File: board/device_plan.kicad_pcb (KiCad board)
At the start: 2 copper layers, 29 parts, among them J1 USB, U1 ATTINY2313, x1 12M

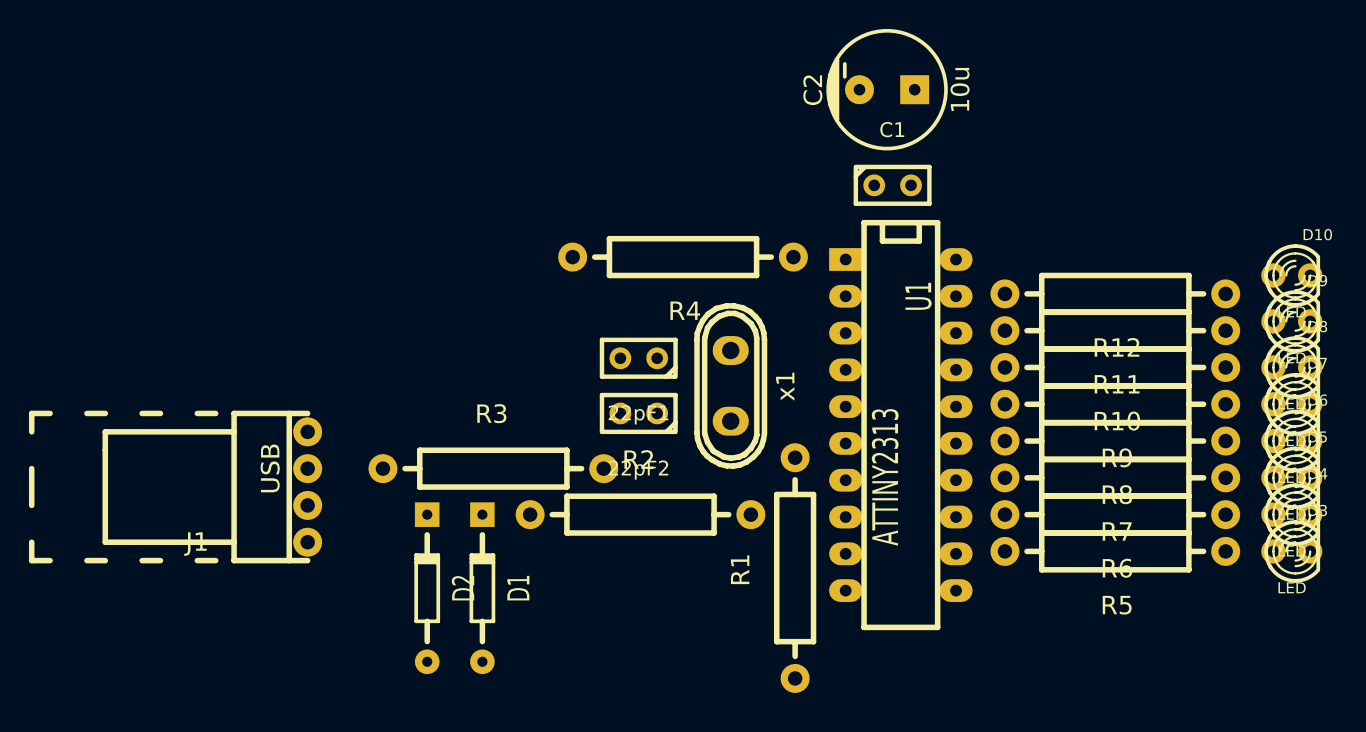
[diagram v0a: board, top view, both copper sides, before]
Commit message: Laid traces on pcb. Added .gitignore.
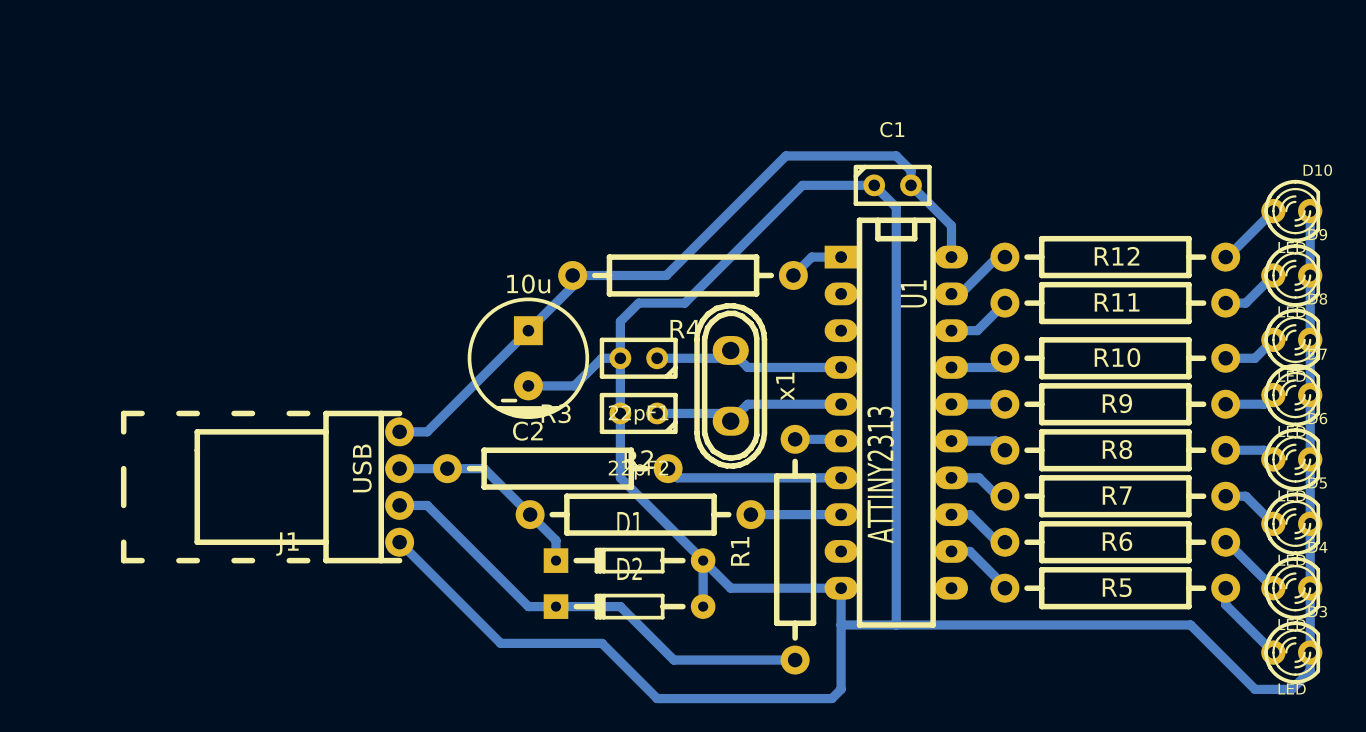
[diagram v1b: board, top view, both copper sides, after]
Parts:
- moved C2 30.9 mm to (119.4, 85.7), turned to 180 degrees
- moved D2 14.0 mm to (126.4, 102.9), turned to 180 degrees
- moved D1 10.3 mm to (126.4, 99.7), turned to 180 degrees
- moved D3 6.98 mm to (172.1, 106.0)
- moved J1 6.35 mm to (110.5, 94.6)
- moved D4 5.08 mm to (172.1, 101.6)
- moved D10 4.45 mm to (172.1, 75.6)
- moved R3 4.44 mm to (121.3, 93.3)
- moved D5 3.17 mm to (172.1, 97.2)
- moved D9 3.17 mm to (172.1, 80.0)
- moved R12 2.54 mm to (160.0, 78.7)
- moved R5 2.54 mm to (160.0, 101.6)
- moved D8 1.91 mm to (172.1, 84.5)
- moved R6 1.91 mm to (160.0, 98.4)
- moved R11 1.90 mm to (160.0, 81.9)
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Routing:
- net GND: track 0.00 -> 200.6 mm
- net VCC: track 0.00 -> 51.2 mm
- net Net-(D2-Pad2): track 0.00 -> 31.7 mm
- net Net-(D1-Pad2): track 0.00 -> 14.2 mm
- net Net-(22pF1-Pad1): track 0.00 -> 13.4 mm
- net Net-(22pF2-Pad1): track 0.00 -> 13.4 mm
- net Net-(R3-Pad2): track 0.00 -> 12.2 mm
- net Net-(R2-Pad2): track 0.00 -> 6.23 mm
- net Net-(D3-Pad1): track 0.00 -> 5.81 mm
- net Net-(R5-Pad2): track 0.00 -> 4.81 mm
- net Net-(R12-Pad2): track 0.00 -> 4.74 mm
- net Net-(D4-Pad1): track 0.00 -> 4.61 mm
- net Net-(D10-Pad1): track 0.00 -> 4.61 mm
- net Net-(R6-Pad2): track 0.00 -> 4.48 mm
- net Net-(R11-Pad2): track 0.00 -> 4.48 mm
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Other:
- net class Default: trace_width 0.254 -> 0.635
